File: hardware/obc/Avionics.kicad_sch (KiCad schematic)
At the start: 42 parts, among them U101 MAX706RESA, U103 RP2350_80QFN, Y101 Crystal_GND24_Small

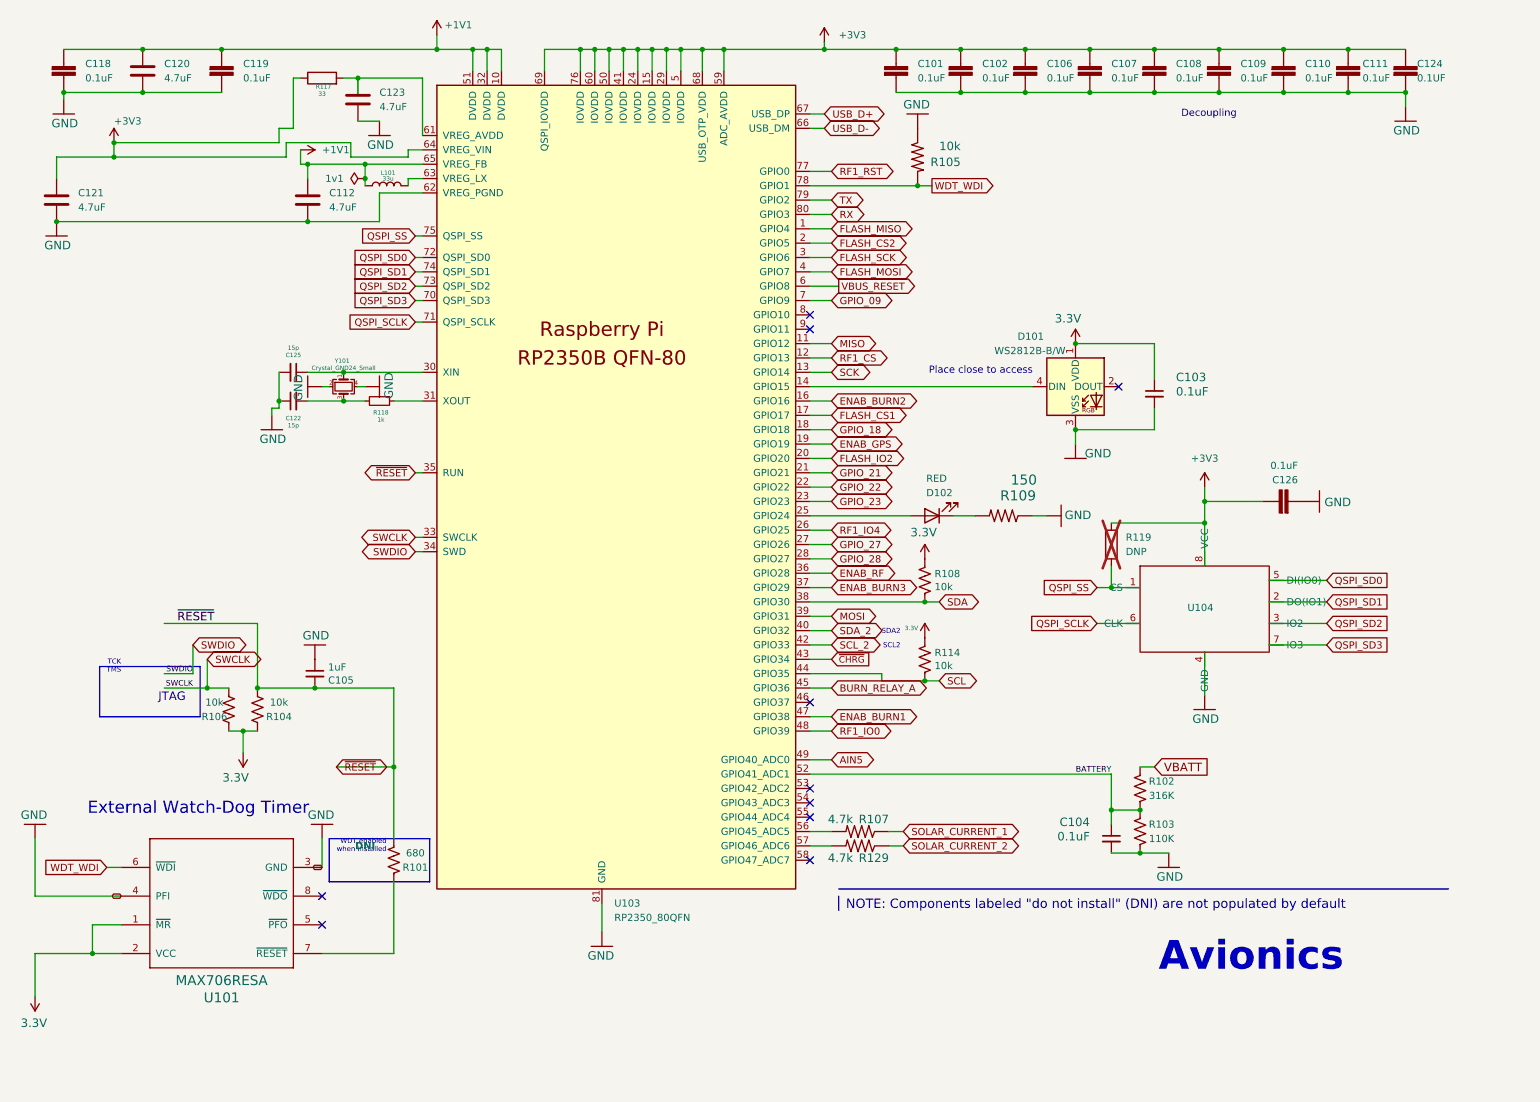
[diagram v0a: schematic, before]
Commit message: OBC: Continuing work towards the next revision
- moved Jtag to Avionics page
- re-aligned and removed excess text
- flipped watchdog to make +3.3v face up
- cleaned up VREG pins, crystal, SWCLK, SWDIO, and watch dog connections
- fixed MRAM symbol
- changed USB_D +/- resistor values
- spaced out schematics on power and burn wire pages
- fixed GNDREF connection for J302
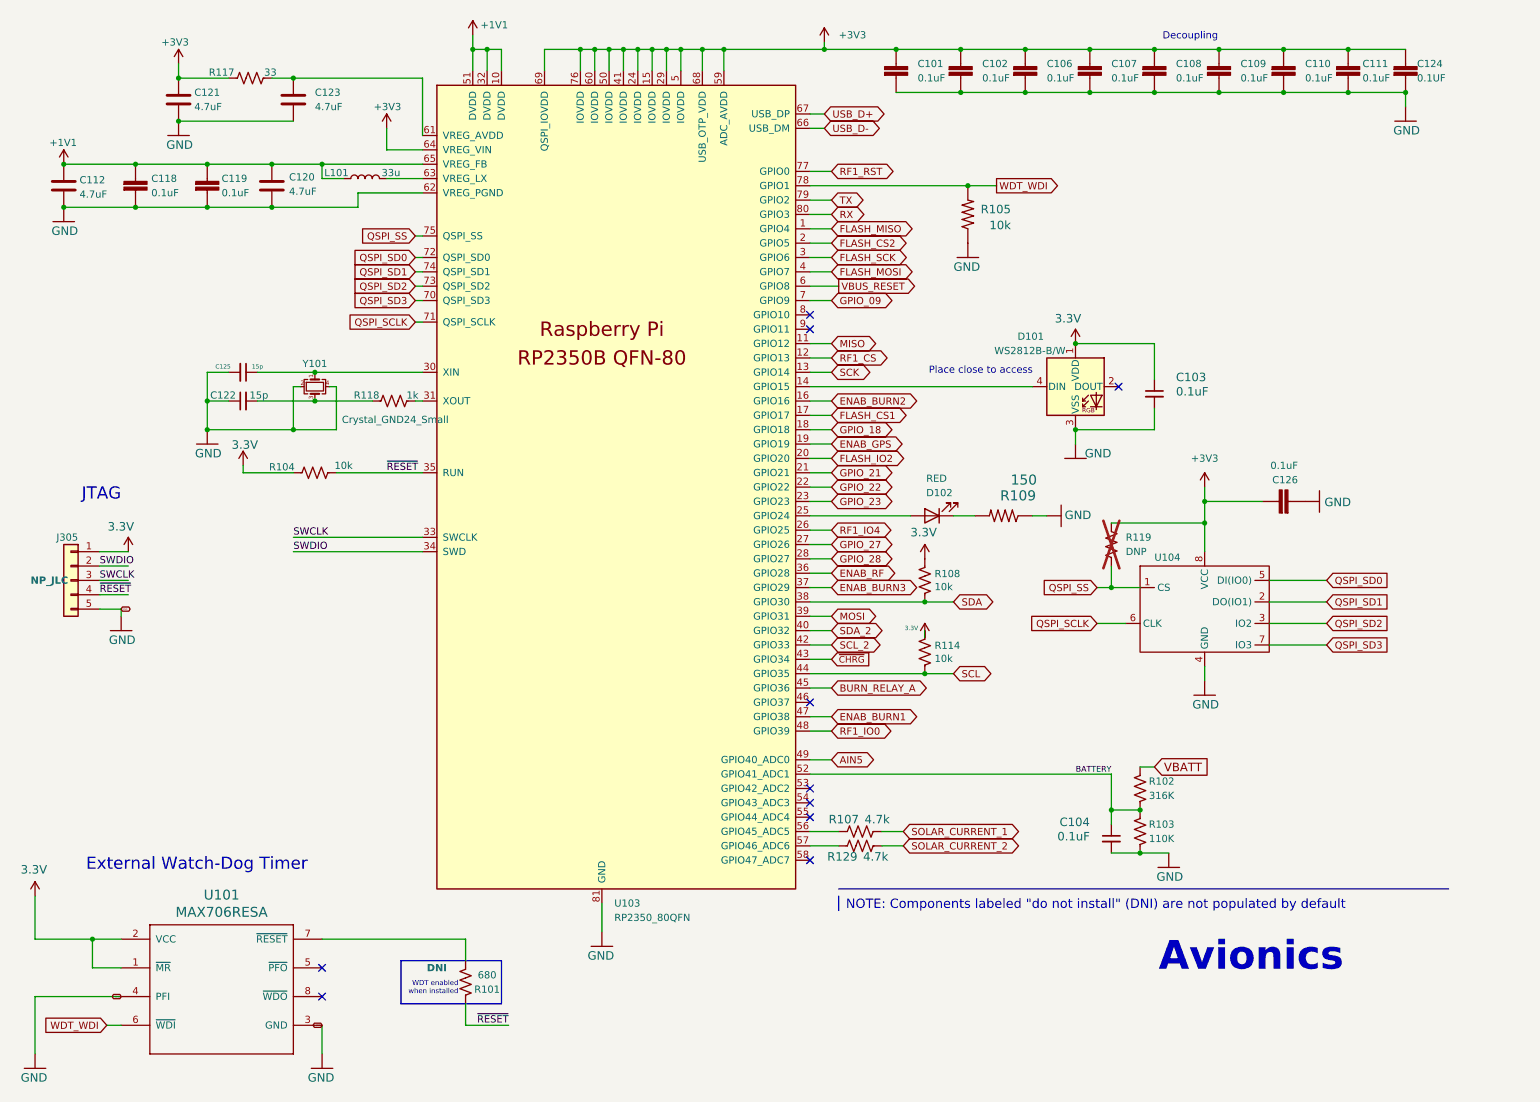
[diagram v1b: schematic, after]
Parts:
- removed C105: 1uF, Capacitor_SMD:C_0603_1608Metric, symbol mainboard:C_Small
- removed R106: 10k, Resistor_SMD:R_0603_1608Metric, symbol Device:R_US
- added J305: Conn_01x05, Connector_PinHeader_2.54mm:PinHeader_1x05_P2.54mm_Vertical, symbol Connector_Generic:Conn_01x05
- R107, R129: symbol mainboard:10KOHM-1_10W-1%(0603)0603 -> Device:R_US
- R117, R119: symbol Device:R -> Device:R_US
- R118: symbol Device:R_Small -> Device:R_US
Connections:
- net 3.3V: now also J305.1 (Pin_1)
- net GND: now also J305.5 (Pin_5)
- net SWCLK: now also J305.3 (Pin_3)
- net SWDIO: now also J305.2 (Pin_2)
- net ~{RESET}: now also R101.2, J305.4 (Pin_4); no longer R101.1
- net at U101.7 (~{RESET}): now also R101.1; no longer R101.2
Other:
- note removed: "SCL2"
- note removed: "SDA2"
- note removed: "TCK TMS"
- moved on the sheet: C112, C118, C119, C120, C121, C122, C123, C125, L101, R101, R105, R114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

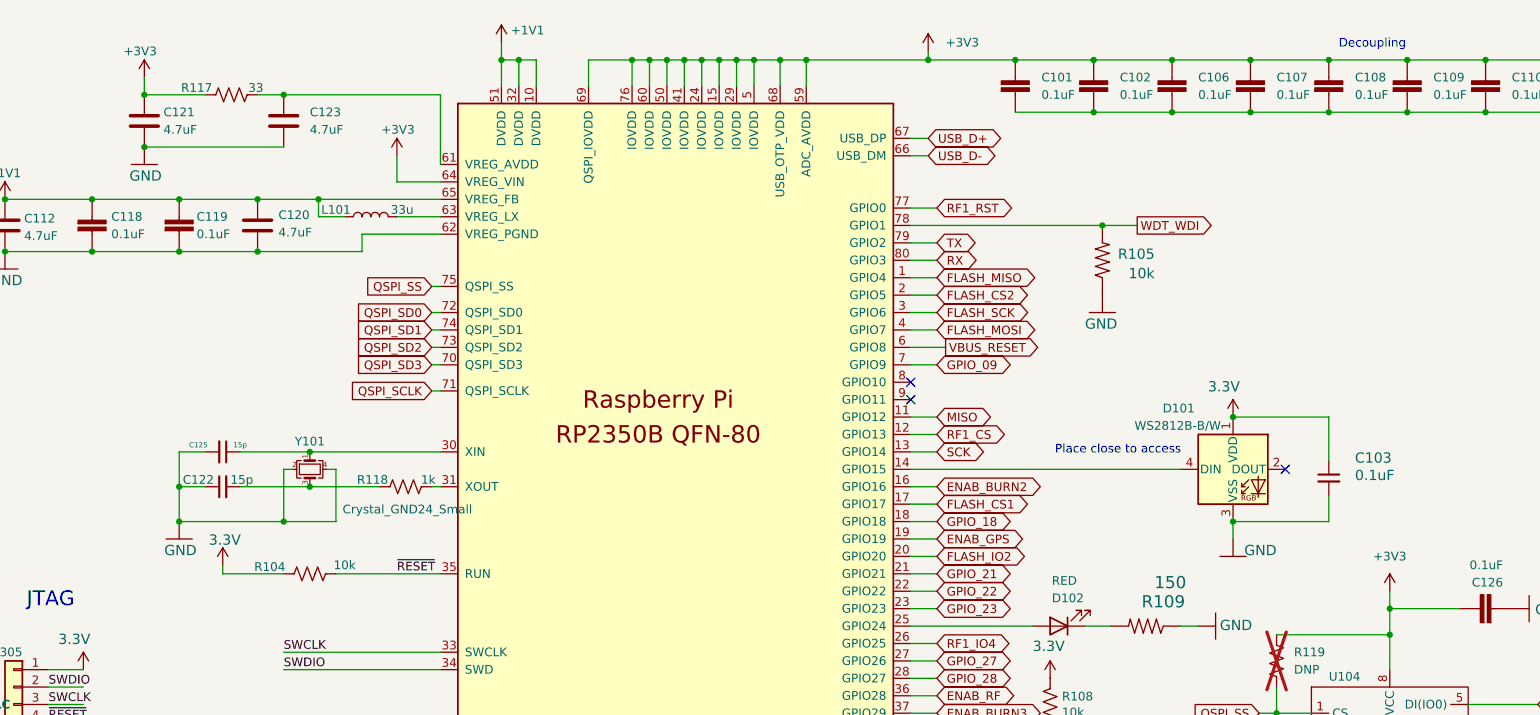
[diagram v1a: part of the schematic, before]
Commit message: OBC: Continuing work towards the next revision
- Changed 3.3V names on Avionics page
- Removed buss protection-bypass jumpers
- Edited SPI buss protection
- Removed U302
- Removed JP401
- Other label/clean up modifications
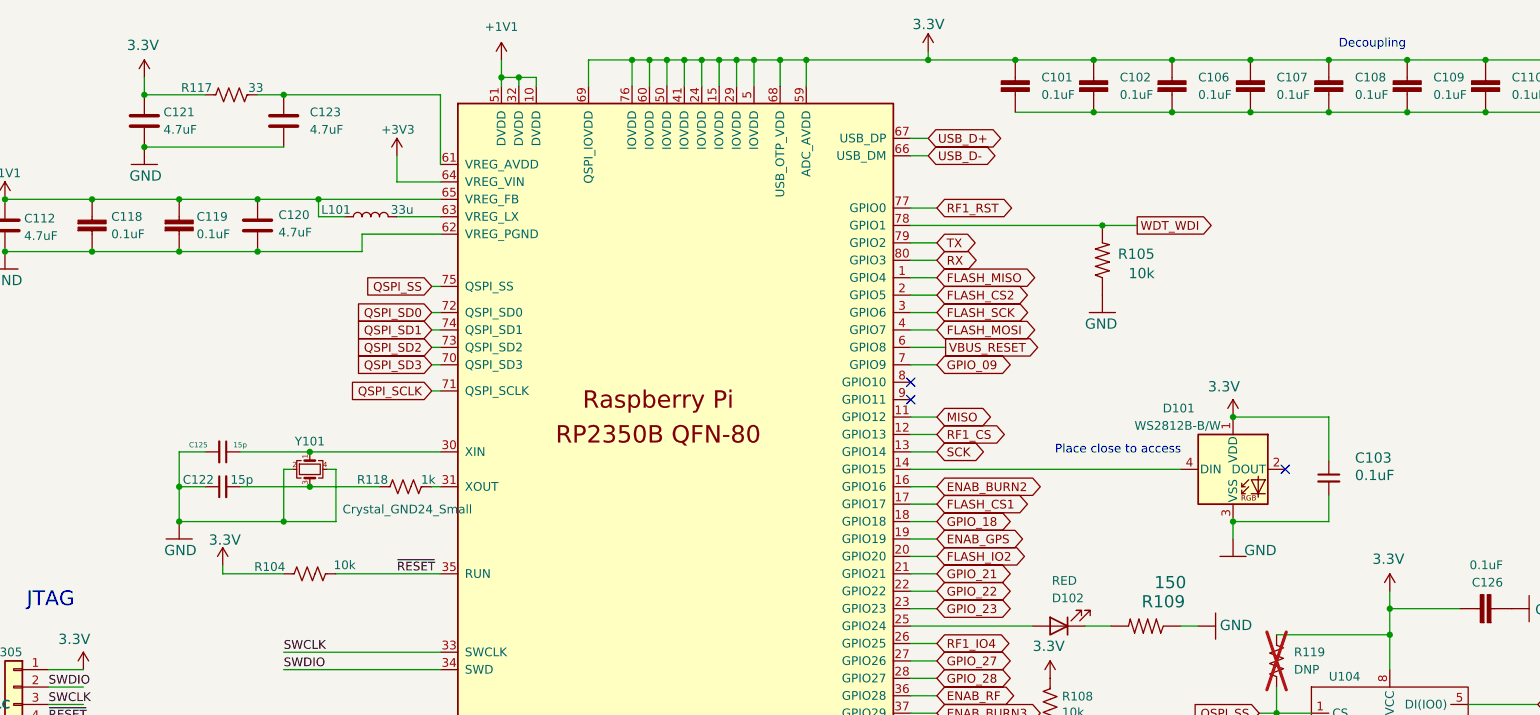
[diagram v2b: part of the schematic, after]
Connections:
- net +3V3: no longer C101.1, C102.1, C106.1, C107.1, C108.1, C109.1, C110.1, C111.1, C121.1, C124.1, C126.1, R117.1, R119.1, U103.15 (IOVDD), U103.24 (IOVDD), U103.29 (IOVDD), U103.41 (IOVDD), U103.5 (IOVDD), U103.50 (IOVDD), U103.59 (ADC_AVDD), U103.60 (IOVDD), U103.68 (USB_OTP_VDD), U103.69 (QSPI_IOVDD), U103.76 (IOVDD), U104.8 (VCC)
- net 3.3V: now also C101.1, C102.1, C106.1, C107.1, C108.1, C109.1, C110.1, C111.1, C121.1, C124.1, C126.1, R117.1, R119.1, U103.15 (IOVDD), U103.24 (IOVDD), U103.29 (IOVDD), U103.41 (IOVDD), U103.5 (IOVDD), U103.50 (IOVDD), U103.59 (ADC_AVDD), U103.60 (IOVDD), U103.68 (USB_OTP_VDD), U103.69 (QSPI_IOVDD), U103.76 (IOVDD), U104.8 (VCC)

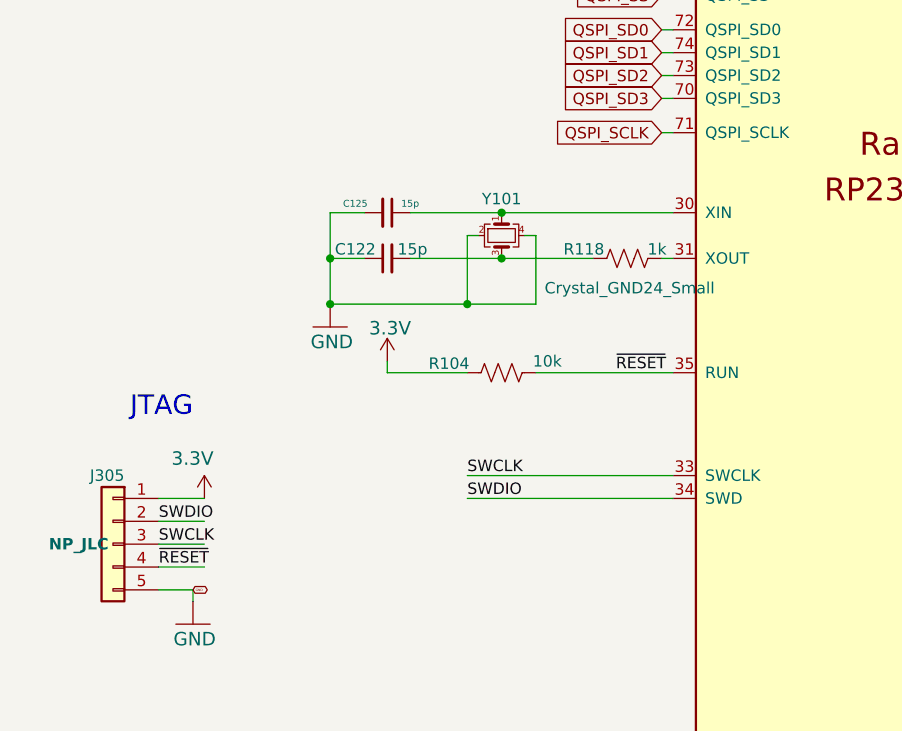
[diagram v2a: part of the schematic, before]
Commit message: OBC: Continuing work towards the next revision
- Cleaned up text on Avionics Page
- Changed some descriptions and cleaned up text on Power Page
- Changed Power Relay A schematic to one from PCB
- Changed R120 and R401 changed from 107k to 34.8k and changed R121 and R404 from 0 to 10k and R127 and R419 from 3.01k to 3.83k (Solar Chargers Page)
- Checked R303 and R304 resistor value and believe 27 is correct
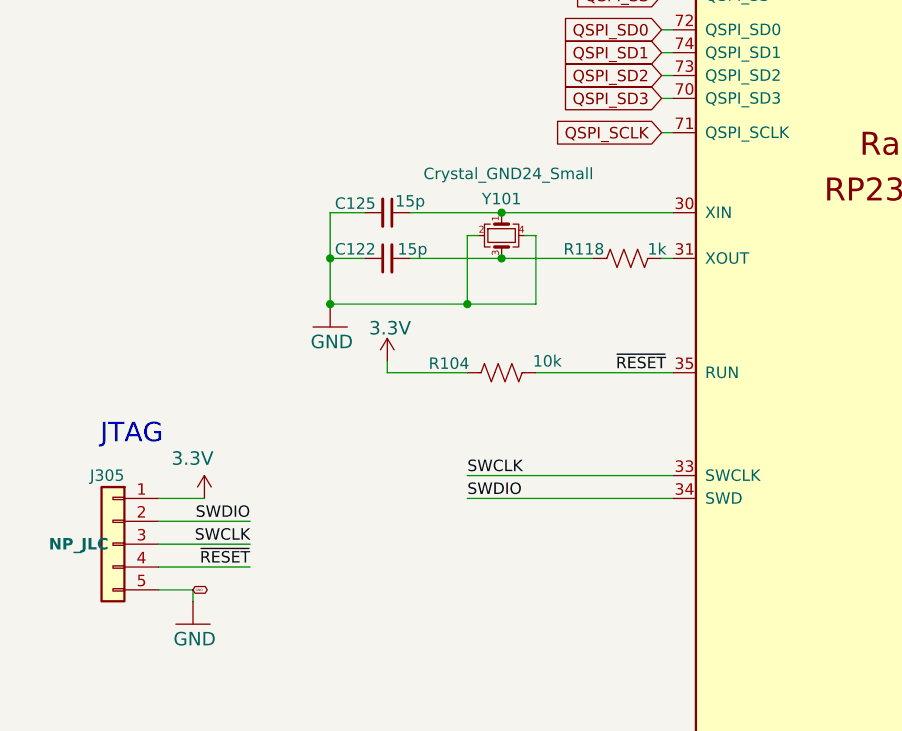
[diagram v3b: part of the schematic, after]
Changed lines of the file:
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@@
 	(wire
 		(pts
-			(xy 27.94 115.57) (xy 33.02 115.57)
-		)
-		(stroke
-			(width 0)
-			(type default)
-		)
-	)
-	(wire
-		(pts
 			(xy 125.73 22.86) (xy 125.73 19.05)
 		)
@@
 	(wire
 		(pts
-			(xy 27.94 110.49) (xy 33.02 110.49)
-		)
-		(stroke
-			(width 0)
-			(type default)
-		)
-	)
-	(wire
-		(pts
 			(xy 67.31 39.37) (xy 85.09 39.37)
 		)
@@
 	(wire
 		(pts
+			(xy 27.94 115.57) (xy 38.1 115.57)
+		)
+		(stroke
+			(width 0)
+			(type default)
+		)
+	)
+	(wire
+		(pts
 			(xy 41.91 21.59) (xy 41.91 24.13)
 		)
@@
 	(wire
 		(pts
-			(xy 27.94 113.03) (xy 33.02 113.03)
+			(xy 58.42 46.99) (xy 46.99 46.99)
 		)
 		(stroke
@@
 	(wire
 		(pts
-			(xy 58.42 46.99) (xy 46.99 46.99)
+			(xy 153.67 96.52) (xy 157.48 96.52)
 		)
 		(stroke
@@
 	(wire
 		(pts
-			(xy 153.67 96.52) (xy 157.48 96.52)
+			(xy 153.67 109.22) (xy 157.48 109.22)
 		)
 		(stroke
@@
 	(wire
 		(pts
-			(xy 153.67 109.22) (xy 157.48 109.22)
+			(xy 138.43 19.05) (xy 138.43 22.86)
 		)
 		(stroke
@@
 	(wire
 		(pts
-			(xy 138.43 19.05) (xy 138.43 22.86)
+			(xy 27.94 113.03) (xy 38.1 113.03)
 		)
 		(stroke
@@
 	(wire
 		(pts
+			(xy 27.94 110.49) (xy 38.1 110.49)
+		)
+		(stroke
+			(width 0)
+			(type default)
+		)
+	)
+	(wire
+		(pts
 			(xy 85.09 36.83) (xy 78.74 36.83)
 		)
@@
 	(text "JTAG"
 		(exclude_from_sim no)
-		(at 31.75 99.06 0)
+		(at 28.448 102.108 0)
 		(effects
 			(font
@@
 	)
 	(label "SWCLK"
-		(at 27.94 113.03 0)
+		(at 38.1 113.03 180)
 		(fields_autoplaced yes)
 		(effects
@@
 				(size 1.27 1.27)
 			)
-			(justify left bottom)
+			(justify right bottom)
 		)
 	)
@@
 	)
 	(label "SWDIO"
-		(at 27.94 110.49 0)
+		(at 38.1 110.49 180)
 		(fields_autoplaced yes)
 		(effects
@@
 				(size 1.27 1.27)
 			)
-			(justify left bottom)
+			(justify right bottom)
 		)
 	)
@@
 	)
 	(label "~{RESET}"
-		(at 27.94 115.57 0)
+		(at 38.1 115.57 180)
 		(fields_autoplaced yes)
 		(effects
@@
 				(size 1.27 1.27)
 			)
-			(justify left bottom)
+			(justify right bottom)
 		)
 	)
@@
 			(effects
 				(font
-					(size 0.762 0.762)
+					(size 1.27 1.27)
 				)
 			)
 		)
 		(property "Value" "15p"
-			(at 55.88 75.184 90)
+			(at 55.88 74.93 90)
 			(effects
 				(font
-					(size 0.762 0.762)
+					(size 1.27 1.27)
 				)
 			)
@@
 		)
 		(property "Value" "Crystal_GND24_Small"
-			(at 80.264 84.582 90)
+			(at 66.802 71.882 90)
 			(effects
 				(font
